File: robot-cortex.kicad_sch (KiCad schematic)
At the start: 10 parts, among them J1 USB4110GFA, U1 DF52-4S-0.8H(21)

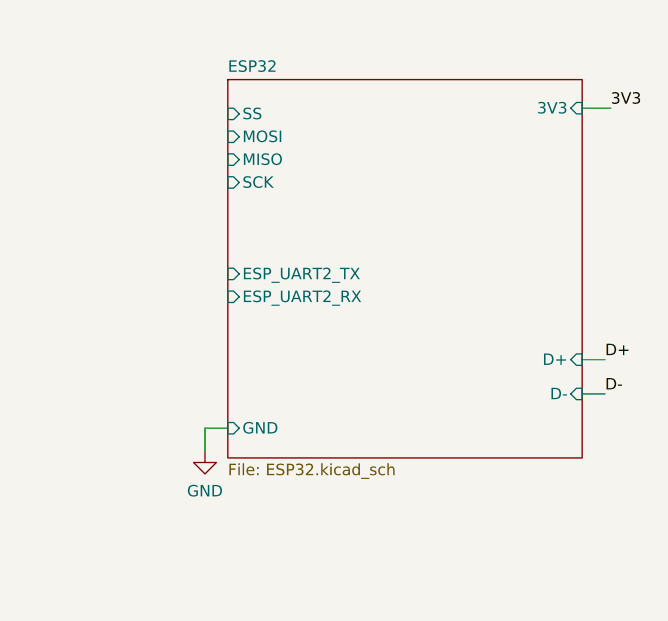
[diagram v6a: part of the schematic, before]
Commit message: heirarchichal sheet label error fix
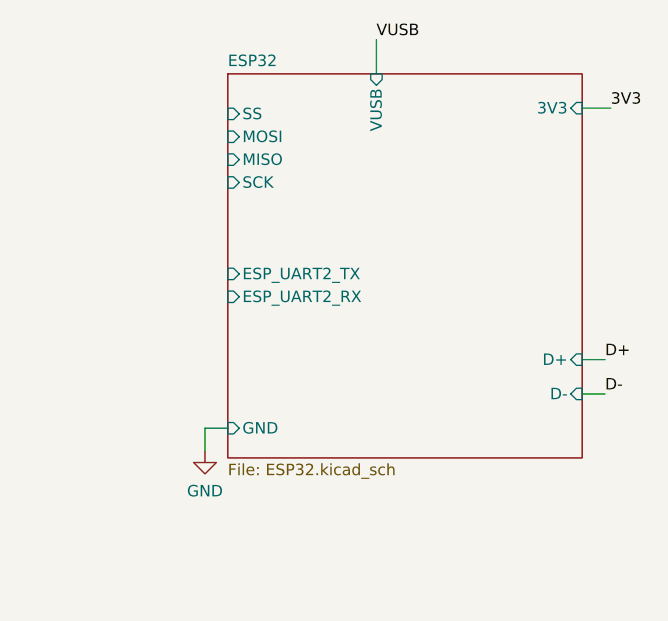
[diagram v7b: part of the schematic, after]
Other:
- sheet ESP32 ports: added VUSB; removed none
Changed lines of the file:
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@@
+    (stroke (width 0) (type default))
+  )
+  (wire (pts (xy 201.93 72.39) (xy 201.93 76.2))
     (stroke (width 0) (type default))
   )
@@
   (label "VBAT" (at 86.36 172.085 180) (fields_autoplaced)
     (effects (font (size 1.27 1.27)) (justify right bottom))
+  )
+  (label "VUSB" (at 201.93 72.39 0) (fields_autoplaced)
+    (effects (font (size 1.27 1.27)) (justify left bottom))
   )
   (label "D-" (at 34.29 165.735 180) (fields_autoplaced)
@@
     )
   )
-  (sheet (at 185.42 76.835) (size 39.37 42.037) (fields_autoplaced)
+  (sheet (at 185.42 76.2) (size 39.37 42.672) (fields_autoplaced)
     (stroke (width 0.1524) (type solid))
     (fill (color 0 0 0 0.0000))
-    (property "Sheetname" "ESP32" (at 185.42 76.1234 0)
+    (property "Sheetname" "ESP32" (at 185.42 75.4884 0)
       (effects (font (size 1.27 1.27)) (justify left bottom))
     )
@@
       (effects (font (size 1.27 1.27)) (justify left top))
     )
-    (property "Field2" "" (at 185.42 76.835 0)
+    (property "Field2" "" (at 185.42 76.2 0)
       (effects (font (size 1.27 1.27)) hide)
     )
@@
       (effects (font (size 1.27 1.27)) (justify right))
     )
+    (pin "VUSB" input (at 201.93 76.2 90)
+      (effects (font (size 1.27 1.27)) (justify right))
+    )

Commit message: sch done sans one additional change, of figuring out how to safely connect VUSB to +5V0 on the CAN transciever
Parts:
- removed U1: DF52-4S-0.8H(21), robot-cortex:DF52-4S-0.8H(21), symbol robot-cortex:DF52-4S-0.8H(21)
- added C12, C14, C16, C18, C20, C22, C24: 100nF, foc-pcb-library:C_0402_1005Metric, symbol foc-pcb:Capacitor
- added C13, C15, C17, C19, C21, C23: C2998534, foc-pcb-library:C_0603_1608Metric, symbol foc-pcb:Capacitor
- added D7: C84264, foc-pcb-library:LED_0603_1608Metric, symbol foc-pcb:LED
- added M1, M2: THRU_HOLE_PAD, symbol foc-pcb:THRU_HOLE_PAD
- added R10: 470, foc-pcb-library:R_0402_1005Metric, symbol foc-pcb:Resistor
- added U1: SPX3819M5-L-5-0, foc-pcb-library:SOT-23-5, symbol foc-pcb:SPX3819M5-L-5-0
- added U10: DF52-4S-0.8H(21), foc-pcb-library:DF52-4S-0.8H(21), symbol foc-pcb:DF52-4S-0.8H(21)
- added U4: C2901617, foc-pcb-library:ECS-1633-480-BN-TR, symbol foc-pcb:OSCILLATOR-4PIN
- added U7: STM32G431CBT6, foc-pcb-library:LQFP48-STM32, symbol foc-pcb:STM32G431CBtx
- added U8: TLE9250XSJXUMA1, foc-pcb-library:SOIC8-TLE5009, symbol foc-pcb:TLE9250XSJXUMA1
- added U9: DF52-3S-0.8H(21), foc-pcb-library:DF52-3S-0.8H(21), symbol foc-pcb:DF52-3S-0.8H(21)
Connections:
- net GND: now also C12.2, C13.2, C14.2, C15.2, C16.2, C17.2, C18.2, C19.2, C20.2, C21.2, C22.2, C23.2, C24.2, R10.2, U1.2 (GND), U10.4, U10.5 (MNT), U10.6 (MNT), U4.2 (GND/Case), U7.19 (VSSA), U7.23 (VSS), U7.35 (VSS), U7.47 (VSS), U8.2 (GND), U8.8 (RM), U9.3, U9.4 (MNT), U9.5 (MNT)
- net VBAT: now also C21.1, C22.1, U1.1 (VIN), U1.3 (EN), U10.1
- net 3V3-Supply/VIN renamed VDD_MIXED
- new net: U4.3 (OUTPUT), U7.5 (PF0-OSC_IN)
- new net: D7.1 (K), R10.1
- new net +3V3: C13.1, C14.1, C15.1, C16.1, C17.1, C18.1, C19.1, C20.1, U4.1 (Enable/Disable), U4.4 (VDD), U7.1 (VBAT), U7.20 (VREF+), U7.21 (VDDA), U7.24 (VDD), U7.36 (VDD), U7.48 (VDD), U8.5 (VIO)
- new net +5V0: C23.1, C24.1, U1.5 (VOUT), U8.3 (Vcc)
- new net BOOT: U7.45 (PB8)
- new net CANH: U10.3, U8.7 (CANH)
- new net CANL: U10.2, U8.6 (CANL)
- new net COS: U7.8 (PA0)
- new net ENABLE: U7.26 (PB12)
- new net FDCAN1_RX: U7.33 (PA11), U8.4 (RxD)
- new net FDCAN1_TX: U7.34 (PA12), U8.1 (TxD)
- new net ISENSE_A: U7.16 (PB0)
- new net ISENSE_B: U7.17 (PB1)
- new net ISENSE_C: U7.25 (PB11)
- new net LED: D7.2 (A), U7.22 (PB10)
- new net NRST: C12.1, U7.7 (PG10-NRST)
- new net SIN: U7.9 (PA1)
- new net SPI1_MISO: U7.41 (PB4)
- new net SPI1_MOSI: U7.42 (PB5)
- new net SPI1_SCK: U7.40 (PB3)
- new net SS: U7.46 (PB9)
- new net SWCLK: U7.38 (PA14), U9.2
- new net SWDIO: U7.37 (PA13), U9.1
- new net UART1_RX: U7.44 (PB7)
- new net UART1_TX: U7.43 (PB6)
- new net UART2_RX: M2.1, U7.11 (PA3)
- new net UART2_TX: M1.1, U7.10 (PA2)
- no-connect marks 2 -> 13
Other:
- sheet ESP32 ports: added BOOT, NRST; removed none
- moved on the sheet: C5, D1, D4, D5, D6, J1, R7, R8
